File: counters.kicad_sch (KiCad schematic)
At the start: 21 parts, among them J10 Conn_01x10_Socket, J11 Conn_01x06_Socket, J12 Conn_01x10_Socket, J13 Conn_01x03_Socket, J8 Conn_01x10_Socket, J9 Conn_01x06_Socket, Q591 DMP3099L, Q592 2N7002, SW1 SW_Push, SW2 SW_Push

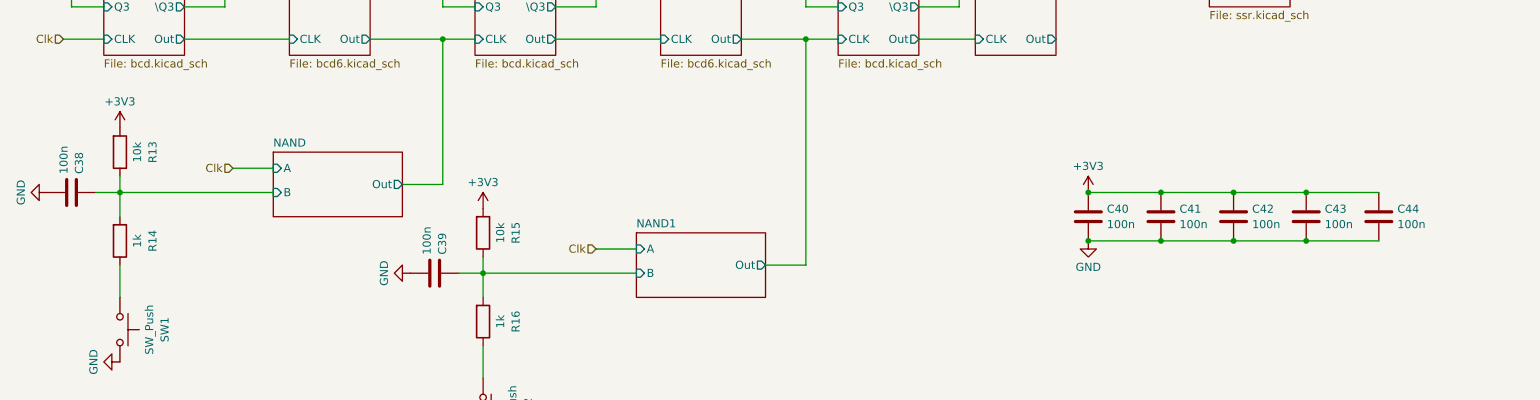
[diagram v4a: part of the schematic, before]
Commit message: started on binary to decimal converter
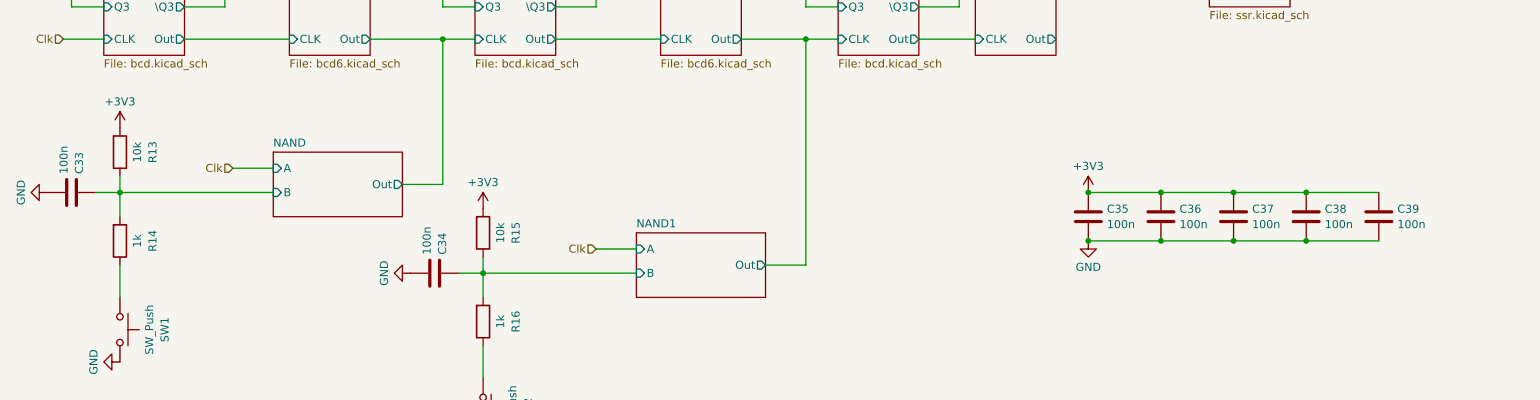
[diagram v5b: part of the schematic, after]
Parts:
- renumbered C38 to C33, C39 to C34, C40 to C35, C41 to C36, C42 to C37, C43 to C38, C44 to C39
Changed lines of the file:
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@@
 		(dnp no)
 		(fields_autoplaced yes)
-		(property "Reference" "#PWR0247"
+		(property "Reference" "#PWR0237"
 			(at 209.55 105.41 0)
 			(effects
@@
 		)
 		(instances
-			(project ""
-				(path "/ce10d5bc-995e-4952-aa76-0a08f713a0f2/2c36a9e9-de42-4705-9ad4-94f4cc168e2f"
-					(reference "#PWR0247")
+			(project "transistor-clock"
+				(path "/ce10d5bc-995e-4952-aa76-0a08f713a0f2/2c36a9e9-de42-4705-9ad4-94f4cc168e2f"
+					(reference "#PWR0237")
 					(unit 1)
 				)
@@
 		(dnp no)
 		(fields_autoplaced yes)
-		(property "Reference" "#PWR0243"
+		(property "Reference" "#PWR0233"
 			(at 90.17 186.69 0)
 			(effects
@@
 			(project "transistor-clock"
 				(path "/ce10d5bc-995e-4952-aa76-0a08f713a0f2/2c36a9e9-de42-4705-9ad4-94f4cc168e2f"
-					(reference "#PWR0243")
+					(reference "#PWR0233")
 					(unit 1)
 				)
@@
 		(dnp no)
 		(fields_autoplaced yes)
-		(property "Reference" "#PWR0240"
+		(property "Reference" "#PWR0230"
 			(at 33.02 173.99 0)
 			(effects
@@
 		)
 		(instances
-			(project ""
-				(path "/ce10d5bc-995e-4952-aa76-0a08f713a0f2/2c36a9e9-de42-4705-9ad4-94f4cc168e2f"
-					(reference "#PWR0240")
+			(project "transistor-clock"
+				(path "/ce10d5bc-995e-4952-aa76-0a08f713a0f2/2c36a9e9-de42-4705-9ad4-94f4cc168e2f"
+					(reference "#PWR0230")
 					(unit 1)
 				)
@@
 		(dnp no)
 		(fields_autoplaced yes)
-		(property "Reference" "#PWR0241"
+		(property "Reference" "#PWR0231"
 			(at 78.74 160.02 0)
 			(effects
@@
 			(project "transistor-clock"
 				(path "/ce10d5bc-995e-4952-aa76-0a08f713a0f2/2c36a9e9-de42-4705-9ad4-94f4cc168e2f"
-					(reference "#PWR0241")
+					(reference "#PWR0231")
 					(unit 1)
 				)
@@
 		)
 		(instances
-			(project ""
+			(project "transistor-clock"
 				(path "/ce10d5bc-995e-4952-aa76-0a08f713a0f2/2c36a9e9-de42-4705-9ad4-94f4cc168e2f"
 					(reference "J9")
@@
 		)
 		(instances
-			(project ""
+			(project "transistor-clock"
 				(path "/ce10d5bc-995e-4952-aa76-0a08f713a0f2/2c36a9e9-de42-4705-9ad4-94f4cc168e2f"
 					(reference "J13")
@@
 		(dnp no)
 		(fields_autoplaced yes)
-		(property "Reference" "C40"
+		(property "Reference" "C35"
 			(at 194.691 149.9178 0)
 			(effects
@@
 			(project "transistor-clock"
 				(path "/ce10d5bc-995e-4952-aa76-0a08f713a0f2/2c36a9e9-de42-4705-9ad4-94f4cc168e2f"
-					(reference "C40")
+					(reference "C35")
 					(unit 1)
 				)
@@
 		)
 		(instances
-			(project ""
+			(project "transistor-clock"
 				(path "/ce10d5bc-995e-4952-aa76-0a08f713a0f2/2c36a9e9-de42-4705-9ad4-94f4cc168e2f"
 					(reference "R13")
@@
 		(dnp no)
 		(fields_autoplaced yes)
-		(property "Reference" "#PWR0246"
+		(property "Reference" "#PWR0236"
 			(at 209.55 82.55 0)
 			(effects
@@
 		)
 		(instances
-			(project ""
-				(path "/ce10d5bc-995e-4952-aa76-0a08f713a0f2/2c36a9e9-de42-4705-9ad4-94f4cc168e2f"
-					(reference "#PWR0246")
+			(project "transistor-clock"
+				(path "/ce10d5bc-995e-4952-aa76-0a08f713a0f2/2c36a9e9-de42-4705-9ad4-94f4cc168e2f"
+					(reference "#PWR0236")
 					(unit 1)
 				)
@@
 		)
 		(instances
-			(project ""
+			(project "transistor-clock"
 				(path "/ce10d5bc-995e-4952-aa76-0a08f713a0f2/2c36a9e9-de42-4705-9ad4-94f4cc168e2f"
 					(reference "R14")
@@
 		(dnp no)
 		(fields_autoplaced yes)
-		(property "Reference" "C39"
+		(property "Reference" "C34"
 			(at 90.1122 157.099 0)
 			(effects
@@
 			(project "transistor-clock"
 				(path "/ce10d5bc-995e-4952-aa76-0a08f713a0f2/2c36a9e9-de42-4705-9ad4-94f4cc168e2f"
-					(reference "C39")
+					(reference "C34")
 					(unit 1)
 				)
@@
 		(dnp no)
 		(fields_autoplaced yes)
-		(property "Reference" "C44"
+		(property "Reference" "C39"
 			(at 240.411 149.9178 0)
 			(effects
@@
 			(project "transistor-clock"
 				(path "/ce10d5bc-995e-4952-aa76-0a08f713a0f2/2c36a9e9-de42-4705-9ad4-94f4cc168e2f"
-					(reference "C44")
+					(reference "C39")
 					(unit 1)
 				)
@@
 		(dnp no)
 		(fields_autoplaced yes)
-		(property "Reference" "#PWR0242"
+		(property "Reference" "#PWR0232"
 			(at 96.52 153.67 0)
 			(effects
@@
 			(project "transistor-clock"
 				(path "/ce10d5bc-995e-4952-aa76-0a08f713a0f2/2c36a9e9-de42-4705-9ad4-94f4cc168e2f"
-					(reference "#PWR0242")
+					(reference "#PWR0232")
 					(unit 1)
 				)
@@
 		(dnp no)
 		(fields_autoplaced yes)
-		(property "Reference" "C42"
+		(property "Reference" "C37"
 			(at 217.551 149.9178 0)
 			(effects
@@
 			(project "transistor-clock"
 				(path "/ce10d5bc-995e-4952-aa76-0a08f713a0f2/2c36a9e9-de42-4705-9ad4-94f4cc168e2f"
-					(reference "C42")
+					(reference "C37")
 					(unit 1)
 				)
@@
 		(dnp no)
 		(fields_autoplaced yes)
-		(property "Reference" "#PWR0245"
+		(property "Reference" "#PWR0235"
 			(at 191.77 161.29 0)
 			(effects
@@
 			(project "transistor-clock"
 				(path "/ce10d5bc-995e-4952-aa76-0a08f713a0f2/2c36a9e9-de42-4705-9ad4-94f4cc168e2f"
-					(reference "#PWR0245")
+					(reference "#PWR0235")
 					(unit 1)
 				)
@@
 		(dnp no)
 		(fields_autoplaced yes)
-		(property "Reference" "#PWR0239"
+		(property "Reference" "#PWR0229"
 			(at 39.37 140.97 0)
 			(effects
@@
 			(project "transistor-clock"
 				(path "/ce10d5bc-995e-4952-aa76-0a08f713a0f2/2c36a9e9-de42-4705-9ad4-94f4cc168e2f"
-					(reference "#PWR0239")
+					(reference "#PWR0229")
 					(unit 1)
 				)
@@
 		(dnp no)
 		(fields_autoplaced yes)
-		(property "Reference" "C41"
+		(property "Reference" "C36"
 			(at 206.121 149.9178 0)
 			(effects
@@
 			(project "transistor-clock"
 				(path "/ce10d5bc-995e-4952-aa76-0a08f713a0f2/2c36a9e9-de42-4705-9ad4-94f4cc168e2f"
-					(reference "C41")
+					(reference "C36")
 					(unit 1)
 				)
@@
 		(dnp no)
 		(fields_autoplaced yes)
-		(property "Reference" "#PWR0238"
+		(property "Reference" "#PWR0228"
 			(at 21.59 147.32 0)
 			(effects
@@
 		)
 		(instances
-			(project ""
-				(path "/ce10d5bc-995e-4952-aa76-0a08f713a0f2/2c36a9e9-de42-4705-9ad4-94f4cc168e2f"
-					(reference "#PWR0238")
+			(project "transistor-clock"
+				(path "/ce10d5bc-995e-4952-aa76-0a08f713a0f2/2c36a9e9-de42-4705-9ad4-94f4cc168e2f"
+					(reference "#PWR0228")
 					(unit 1)
 				)
@@
 		(dnp no)
 		(fields_autoplaced yes)
-		(property "Reference" "C43"
+		(property "Reference" "C38"
 			(at 228.981 149.9178 0)
 			(effects
@@
 			(project "transistor-clock"
 				(path "/ce10d5bc-995e-4952-aa76-0a08f713a0f2/2c36a9e9-de42-4705-9ad4-94f4cc168e2f"
-					(reference "C43")
+					(reference "C38")
 					(unit 1)
 				)
@@
 		)
 		(instances
-			(project ""
+			(project "transistor-clock"
 				(path "/ce10d5bc-995e-4952-aa76-0a08f713a0f2/2c36a9e9-de42-4705-9ad4-94f4cc168e2f"
 					(reference "SW1")
@@
 		(dnp no)
 		(fields_autoplaced yes)
-		(property "Reference" "#PWR0244"
+		(property "Reference" "#PWR0234"
 			(at 191.77 151.13 0)
 			(effects
@@
 			(project "transistor-clock"
 				(path "/ce10d5bc-995e-4952-aa76-0a08f713a0f2/2c36a9e9-de42-4705-9ad4-94f4cc168e2f"
-					(reference "#PWR0244")
+					(reference "#PWR0234")
 					(unit 1)
 				)
@@
 		(dnp no)
 		(fields_autoplaced yes)
-		(property "Reference" "C38"
+		(property "Reference" "C33"
 			(at 32.9622 144.399 0)
 			(effects
@@
 		)
 		(instances
-			(project ""
-				(path "/ce10d5bc-995e-4952-aa76-0a08f713a0f2/2c36a9e9-de42-4705-9ad4-94f4cc168e2f"
-					(reference "C38")
+			(project "transistor-clock"
+				(path "/ce10d5bc-995e-4952-aa76-0a08f713a0f2/2c36a9e9-de42-4705-9ad4-94f4cc168e2f"
+					(reference "C33")
 					(unit 1)
 				)
@@
 		)
 		(instances
-			(project ""
+			(project "transistor-clock"
 				(path "/ce10d5bc-995e-4952-aa76-0a08f713a0f2/2c36a9e9-de42-4705-9ad4-94f4cc168e2f"
 					(reference "J8")

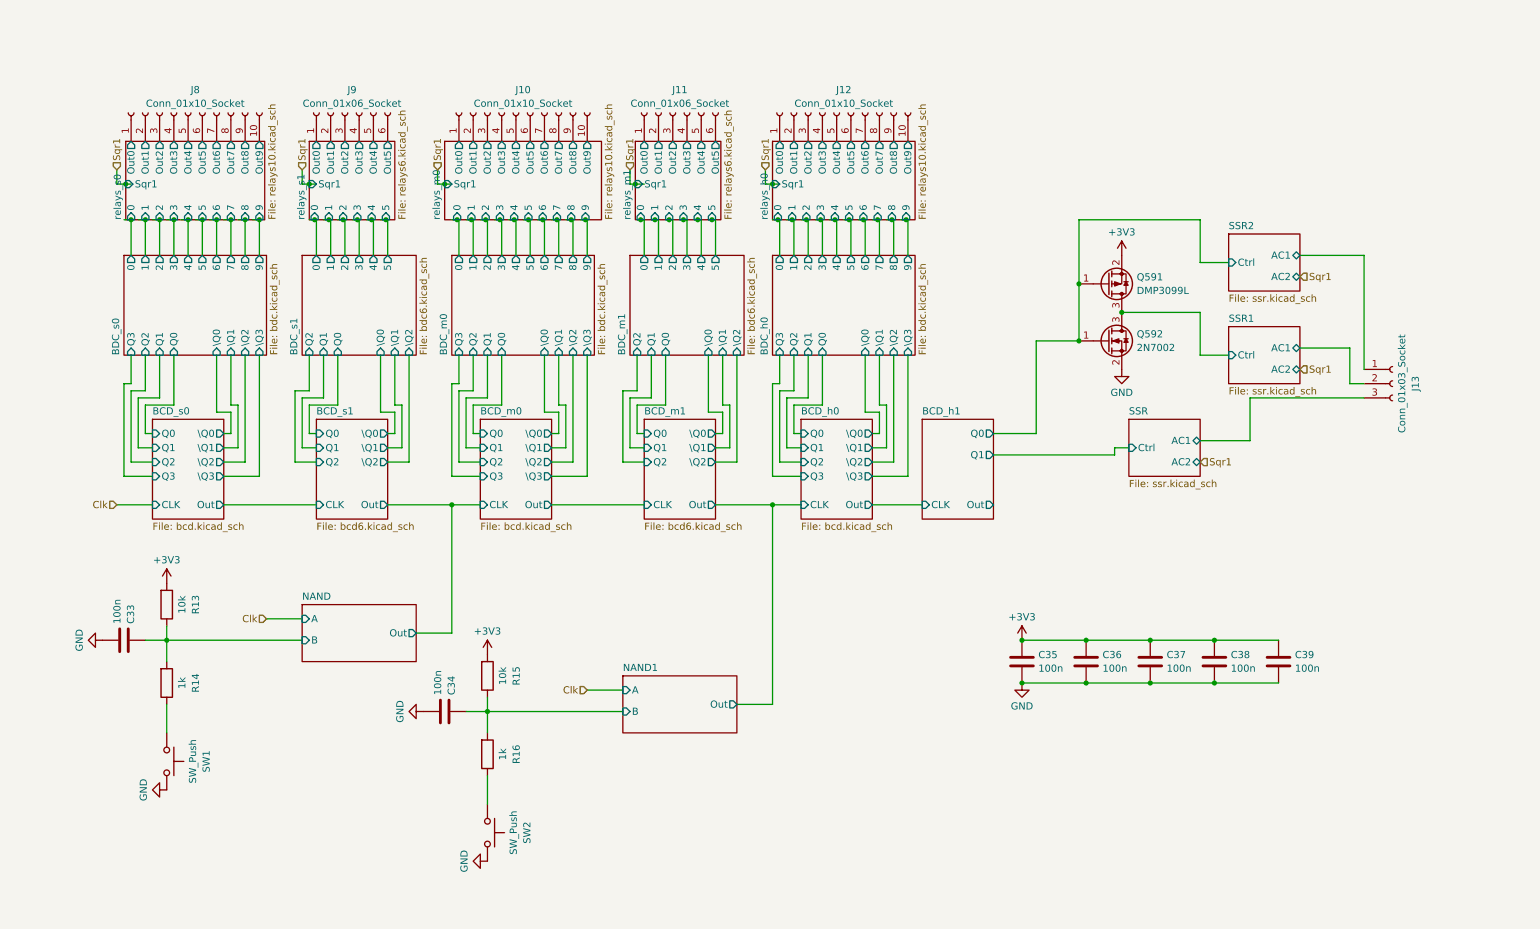
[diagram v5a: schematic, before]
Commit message: replace bcd logic with bin-to-dec module
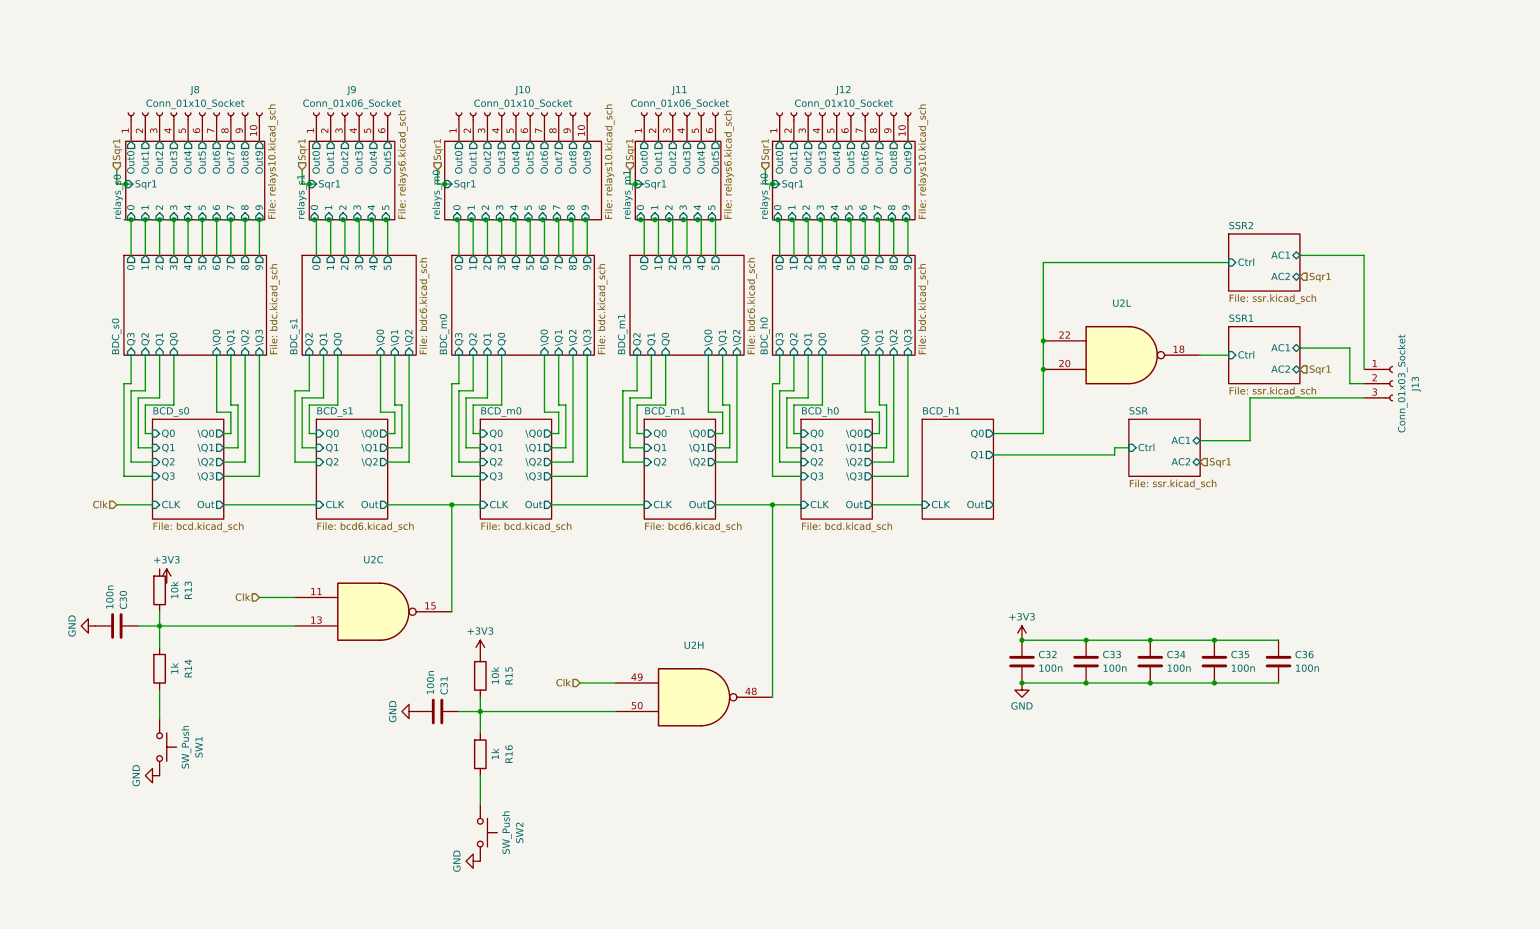
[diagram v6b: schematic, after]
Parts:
- removed Q591: DMP3099L, Package_TO_SOT_SMD:SOT-23, symbol Transistor_FET:DMP3099L
- removed Q592: 2N7002, Package_TO_SOT_SMD:SOT-23, symbol Transistor_FET:2N7002
- added U2: ~, symbol custom:BDC_nands
- renumbered C33 to C30, C34 to C31, C35 to C32, C36 to C33, C37 to C34, C38 to C35, C39 to C36
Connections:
- net +3V3: no longer R13.2
- net BCD_h0/CLK: now also U2.48
- net BCD_h1/Q0: now also U2.20, U2.22
- net BCD_m0/CLK: now also U2.15
- net Clk: now also U2.11, U2.49
- net SSR1/Ctrl: now also U2.18
- net NAND/B: no longer names the net of C30.1, R13.1, R14.2
- net NAND/B: now also U2.13
- net NAND1/B: no longer names the net of C31.1, R15.1, R16.2
- net NAND1/B: now also U2.50
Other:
- removed sheet NAND
- removed sheet NAND1
- moved on the sheet: C30, C31, R13, R14, R15, R16, SW1, SW2

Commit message: switched to using flipflop module
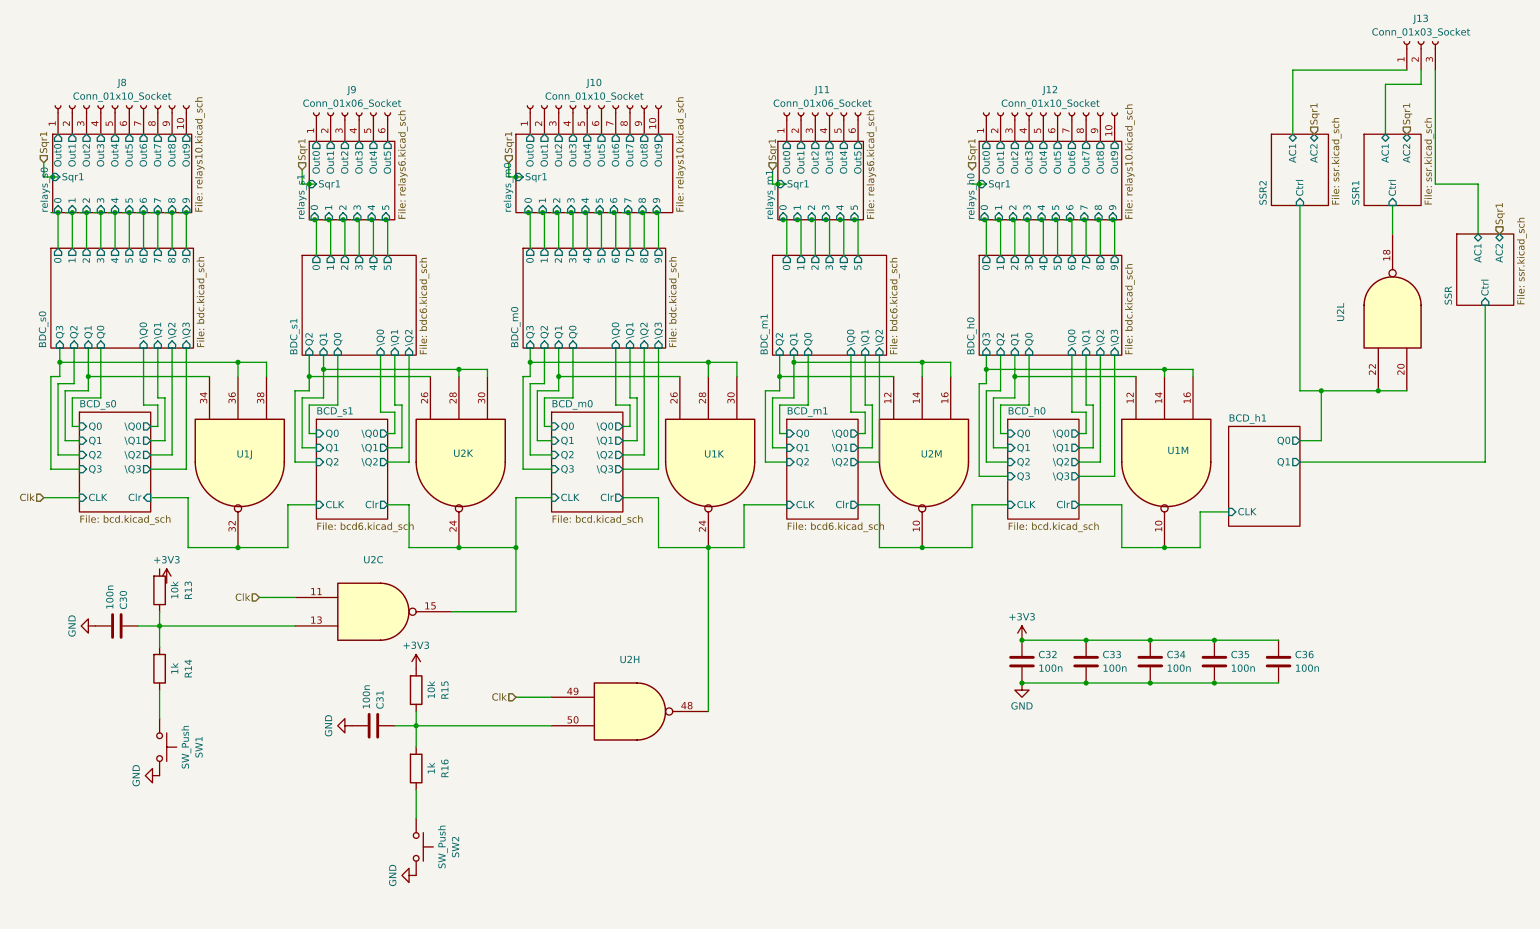
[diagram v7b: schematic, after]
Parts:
- added U1: ~, symbol custom:BDC_nands
- added unit 11 of U2
- added unit 13 of U2
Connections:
- net BCD_h0/CLK: now also U2.10; no longer U2.48
- net BCD_h0/Q1: now also U1.12
- net BCD_h0/Q3: now also U1.14, U1.16
- net BCD_m0/CLK: now also U2.24
- net BCD_m0/Q1: now also U1.26
- net BCD_m0/Q3: now also U1.28, U1.30
- net BCD_m1/Q1: now also U2.14, U2.16
- net BCD_m1/Q2: now also U2.12
- net BCD_s0/Q1: now also U1.34
- net BCD_s0/Q3: now also U1.36, U1.38
- net BCD_s1/Q1: now also U2.28, U2.30
- net BCD_s1/Q2: now also U2.26
- new net BCD_h0/Clr: U1.10
- new net BCD_m0/Clr: U1.24, U2.48
- new net BCD_s1/CLK: U1.32
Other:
- sheet BCD_h0 ports: added Clr; removed Out
- sheet BCD_h1 ports: added none; removed Out
- sheet BCD_m0 ports: added Clr; removed Out
- sheet BCD_m1 ports: added Clr; removed Out
- sheet BCD_s0 ports: added Clr; removed Out
- sheet BCD_s1 ports: added Clr; removed Out
- moved on the sheet: C31, J10, J11, J12, J13, J8, R15, R16, SW2, U2H, U2L
